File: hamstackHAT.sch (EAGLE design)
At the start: 14 parts, among them K2 RASPI_HEADER, U1 TXB0108PWR

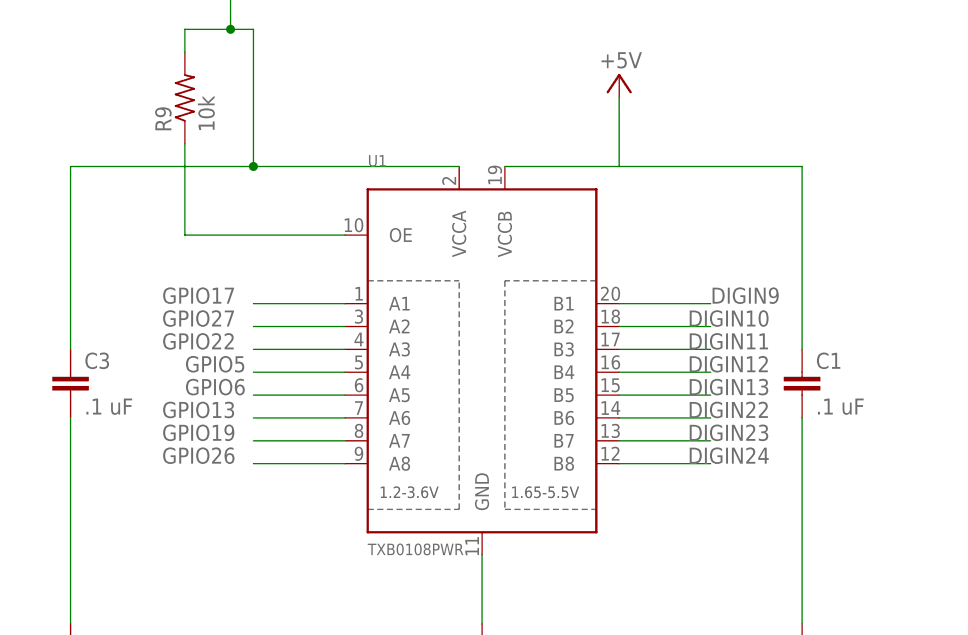
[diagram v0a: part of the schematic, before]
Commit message: re-arange everythign to imporove routing
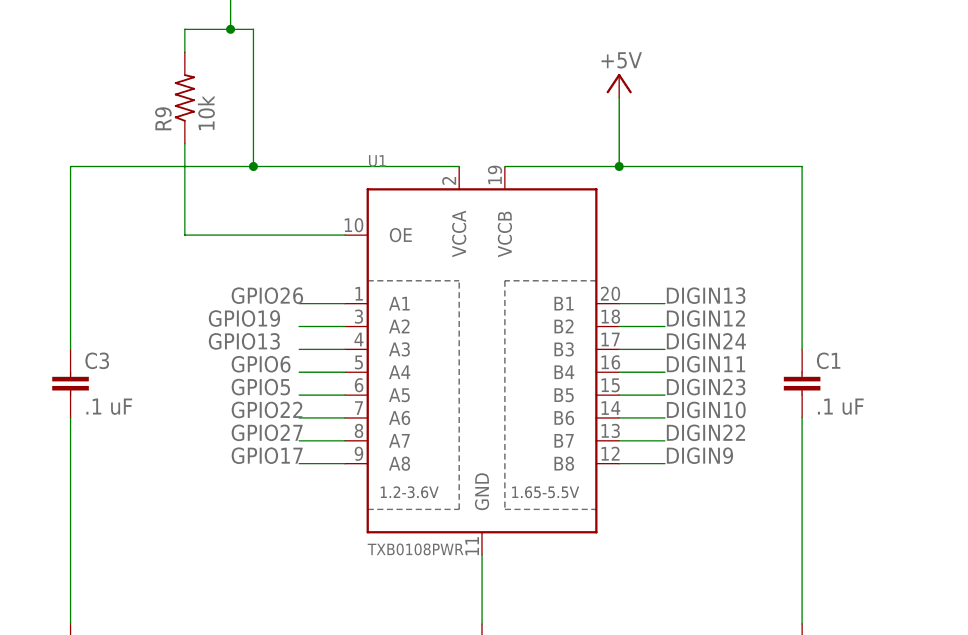
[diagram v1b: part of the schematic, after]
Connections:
- net DIGIN10: now also U1.B6; no longer U1.B2
- net DIGIN11: now also U1.B4; no longer U1.B3
- net DIGIN12: now also U1.B2; no longer U1.B4
- net DIGIN13: now also U1.B1; no longer U1.B5
- net DIGIN22: now also U1.B7; no longer U1.B6
- net DIGIN23: now also U1.B5; no longer U1.B7
- net DIGIN24: now also U1.B3; no longer U1.B8
- net DIGIN9: now also U1.B8; no longer U1.B1
- net GPIO13: now also U1.A3; no longer U1.A6
- net GPIO17: now also U1.A8; no longer U1.A1
- net GPIO19: now also U1.A2; no longer U1.A7
- net GPIO22: now also U1.A6; no longer U1.A3
- net GPIO26: now also U1.A1; no longer U1.A8
- net GPIO27: now also U1.A7; no longer U1.A2
- net GPIO5: now also U1.A5; no longer U1.A4
- net GPIO6: now also U1.A4; no longer U1.A5
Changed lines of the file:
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@@
 <pinref part="P+2" gate="1" pin="+5V"/>
 <pinref part="C1" gate="G$1" pin="1"/>
+<junction x="182.88" y="139.7"/>
 </segment>
 </net>
@@
 </segment>
 <segment>
-<wire x1="182.88" y1="124.46" x2="193.04" y2="124.46" width="0.1524" layer="91"/>
-<pinref part="U1" gate="G$1" pin="B1"/>
-<label x="193.04" y="124.46" size="1.778" layer="95"/>
+<pinref part="U1" gate="G$1" pin="B8"/>
+<wire x1="182.88" y1="106.68" x2="187.96" y2="106.68" width="0.1524" layer="91"/>
+<label x="187.96" y="106.68" size="1.778" layer="95"/>
 </segment>
 </net>
@@
 </segment>
 <segment>
-<wire x1="182.88" y1="121.92" x2="193.04" y2="121.92" width="0.1524" layer="91"/>
-<pinref part="U1" gate="G$1" pin="B2"/>
-<label x="190.5" y="121.92" size="1.778" layer="95"/>
+<pinref part="U1" gate="G$1" pin="B6"/>
+<wire x1="182.88" y1="111.76" x2="187.96" y2="111.76" width="0.1524" layer="91"/>
+<label x="187.96" y="111.76" size="1.778" layer="95"/>
 </segment>
 </net>
@@
 </segment>
 <segment>
-<wire x1="182.88" y1="116.84" x2="193.04" y2="116.84" width="0.1524" layer="91"/>
-<pinref part="U1" gate="G$1" pin="B4"/>
-<label x="190.5" y="116.84" size="1.778" layer="95"/>
+<pinref part="U1" gate="G$1" pin="B2"/>
+<wire x1="182.88" y1="121.92" x2="187.96" y2="121.92" width="0.1524" layer="91"/>
+<label x="187.96" y="121.92" size="1.778" layer="95"/>
 </segment>
 </net>
@@
 </segment>
 <segment>
-<wire x1="182.88" y1="114.3" x2="193.04" y2="114.3" width="0.1524" layer="91"/>
-<pinref part="U1" gate="G$1" pin="B5"/>
-<label x="190.5" y="114.3" size="1.778" layer="95"/>
+<pinref part="U1" gate="G$1" pin="B1"/>
+<wire x1="182.88" y1="124.46" x2="187.96" y2="124.46" width="0.1524" layer="91"/>
+<label x="187.96" y="124.46" size="1.778" layer="95"/>
 </segment>
 </net>
@@
 </segment>
 <segment>
-<wire x1="182.88" y1="109.22" x2="193.04" y2="109.22" width="0.1524" layer="91"/>
-<pinref part="U1" gate="G$1" pin="B7"/>
-<label x="190.5" y="109.22" size="1.778" layer="95"/>
+<pinref part="U1" gate="G$1" pin="B5"/>
+<wire x1="182.88" y1="114.3" x2="187.96" y2="114.3" width="0.1524" layer="91"/>
+<label x="187.96" y="114.3" size="1.778" layer="95"/>
 </segment>
 </net>
@@
 </segment>
 <segment>
-<wire x1="182.88" y1="106.68" x2="193.04" y2="106.68" width="0.1524" layer="91"/>
-<pinref part="U1" gate="G$1" pin="B8"/>
-<label x="190.5" y="106.68" size="1.778" layer="95"/>
+<pinref part="U1" gate="G$1" pin="B3"/>
+<wire x1="182.88" y1="119.38" x2="187.96" y2="119.38" width="0.1524" layer="91"/>
+<label x="187.96" y="119.38" size="1.778" layer="95"/>
 </segment>
 </net>
@@
 </segment>
 <segment>
-<wire x1="182.88" y1="119.38" x2="193.04" y2="119.38" width="0.1524" layer="91"/>
-<pinref part="U1" gate="G$1" pin="B3"/>
-<label x="190.5" y="119.38" size="1.778" layer="95"/>
+<pinref part="U1" gate="G$1" pin="B4"/>
+<wire x1="182.88" y1="116.84" x2="187.96" y2="116.84" width="0.1524" layer="91"/>
+<label x="187.96" y="116.84" size="1.778" layer="95"/>
 </segment>
 </net>
 <net name="DIGIN22" class="0">
-<segment>
-<wire x1="182.88" y1="111.76" x2="193.04" y2="111.76" width="0.1524" layer="91"/>
-<pinref part="U1" gate="G$1" pin="B6"/>
-<label x="190.5" y="111.76" size="1.778" layer="95"/>
-</segment>
 <segment>
 <pinref part="X1" gate="G$1" pin="22"/>
@@
 <label x="152.4" y="180.34" size="1.778" layer="95"/>
 </segment>
+<segment>
+<pinref part="U1" gate="G$1" pin="B7"/>
+<wire x1="182.88" y1="109.22" x2="187.96" y2="109.22" width="0.1524" layer="91"/>
+<label x="187.96" y="109.22" size="1.778" layer="95"/>
+</segment>
 </net>
 <net name="GPIO27" class="0">
-<segment>
-<wire x1="152.4" y1="121.92" x2="142.24" y2="121.92" width="0.1524" layer="91"/>
-<pinref part="U1" gate="G$1" pin="A2"/>
-<label x="132.08" y="121.92" size="1.778" layer="95"/>
-</segment>
 <segment>
 <pinref part="K2" gate="G$1" pin="13"/>
@@
 <label x="10.16" y="160.02" size="1.778" layer="95"/>
 </segment>
+<segment>
+<pinref part="U1" gate="G$1" pin="A7"/>
+<wire x1="147.32" y1="109.22" x2="152.4" y2="109.22" width="0.1524" layer="91"/>
+<label x="139.7" y="109.22" size="1.778" layer="95"/>
+</segment>
 </net>
 <net name="GPIO22" class="0">
-<segment>
-<wire x1="152.4" y1="119.38" x2="142.24" y2="119.38" width="0.1524" layer="91"/>
-<pinref part="U1" gate="G$1" pin="A3"/>
-<label x="132.08" y="119.38" size="1.778" layer="95"/>
-</segment>
 <segment>
 <pinref part="K2" gate="G$1" pin="15"/>
@@
 <label x="7.62" y="157.48" size="1.778" layer="95"/>
 </segment>
+<segment>
+<pinref part="U1" gate="G$1" pin="A6"/>
+<wire x1="147.32" y1="111.76" x2="152.4" y2="111.76" width="0.1524" layer="91"/>
+<label x="139.7" y="111.76" size="1.778" layer="95"/>
+</segment>
 </net>
 <net name="GPIO5" class="0">
-<segment>
-<wire x1="152.4" y1="116.84" x2="142.24" y2="116.84" width="0.1524" layer="91"/>
-<pinref part="U1" gate="G$1" pin="A4"/>
-<label x="134.62" y="116.84" size="1.778" layer="95"/>
-</segment>
 <segment>
 <pinref part="K2" gate="G$1" pin="29"/>
@@
 <label x="10.16" y="139.7" size="1.778" layer="95"/>
 </segment>
+<segment>
+<pinref part="U1" gate="G$1" pin="A5"/>
+<wire x1="147.32" y1="114.3" x2="152.4" y2="114.3" width="0.1524" layer="91"/>
+<label x="139.7" y="114.3" size="1.778" layer="95"/>
+</segment>
 </net>
 <net name="GPIO6" class="0">
-<segment>
-<wire x1="152.4" y1="114.3" x2="142.24" y2="114.3" width="0.1524" layer="91"/>
-<pinref part="U1" gate="G$1" pin="A5"/>
-<label x="134.62" y="114.3" size="1.778" layer="95"/>
-</segment>
 <segment>
 <pinref part="K2" gate="G$1" pin="31"/>
@@
 <label x="12.7" y="137.16" size="1.778" layer="95"/>
 </segment>
+<segment>
+<pinref part="U1" gate="G$1" pin="A4"/>
+<wire x1="147.32" y1="116.84" x2="152.4" y2="116.84" width="0.1524" layer="91"/>
+<label x="139.7" y="116.84" size="1.778" layer="95"/>
+</segment>
 </net>
 <net name="GPIO13" class="0">
-<segment>
-<wire x1="152.4" y1="111.76" x2="142.24" y2="111.76" width="0.1524" layer="91"/>
-<pinref part="U1" gate="G$1" pin="A6"/>
-<label x="132.08" y="111.76" size="1.778" layer="95"/>
-</segment>
 <segment>
 <pinref part="K2" gate="G$1" pin="33"/>
@@
 <label x="7.62" y="134.62" size="1.778" layer="95"/>
 </segment>
+<segment>
+<pinref part="U1" gate="G$1" pin="A3"/>
+<wire x1="147.32" y1="119.38" x2="152.4" y2="119.38" width="0.1524" layer="91"/>
+<label x="137.16" y="119.38" size="1.778" layer="95"/>
+</segment>
 </net>
 <net name="GPIO19" class="0">
-<segment>
-<wire x1="152.4" y1="109.22" x2="142.24" y2="109.22" width="0.1524" layer="91"/>
-<pinref part="U1" gate="G$1" pin="A7"/>
-<label x="132.08" y="109.22" size="1.778" layer="95"/>
-</segment>
 <segment>
 <pinref part="K2" gate="G$1" pin="35"/>
@@
 <label x="10.16" y="132.08" size="1.778" layer="95"/>
 </segment>
+<segment>
+<pinref part="U1" gate="G$1" pin="A2"/>
+<wire x1="147.32" y1="121.92" x2="152.4" y2="121.92" width="0.1524" layer="91"/>
+<label x="137.16" y="121.92" size="1.778" layer="95"/>
+</segment>
 </net>
 <net name="GPIO26" class="0">
-<segment>
-<wire x1="152.4" y1="106.68" x2="142.24" y2="106.68" width="0.1524" layer="91"/>
-<pinref part="U1" gate="G$1" pin="A8"/>
-<label x="132.08" y="106.68" size="1.778" layer="95"/>
-</segment>
 <segment>
 <pinref part="K2" gate="G$1" pin="37"/>
 <wire x1="43.18" y1="129.54" x2="15.24" y2="129.54" width="0.1524" layer="91"/>
 <label x="10.16" y="129.54" size="1.778" layer="95"/>
+</segment>
+<segment>
+<pinref part="U1" gate="G$1" pin="A1"/>
+<wire x1="147.32" y1="124.46" x2="152.4" y2="124.46" width="0.1524" layer="91"/>
+<label x="139.7" y="124.46" size="1.778" layer="95"/>
 </segment>
 </net>
@@
 <net name="GPIO17" class="0">
 <segment>
-<pinref part="U1" gate="G$1" pin="A1"/>
-<wire x1="152.4" y1="124.46" x2="142.24" y2="124.46" width="0.1524" layer="91"/>
-<label x="132.08" y="124.46" size="1.778" layer="95"/>
-</segment>
-<segment>
 <pinref part="K2" gate="G$1" pin="11"/>
 <wire x1="43.18" y1="162.56" x2="17.78" y2="162.56" width="0.1524" layer="91"/>
 <label x="10.16" y="162.56" size="1.778" layer="95"/>
 </segment>
+<segment>
+<pinref part="U1" gate="G$1" pin="A8"/>
+<wire x1="152.4" y1="106.68" x2="147.32" y2="106.68" width="0.1524" layer="91"/>
+<label x="139.7" y="106.68" size="1.778" layer="95"/>
+</segment>
 </net>
 </nets>
 </sheet>
 </sheets>
+<errors>
+</errors>
 </schematic>
 </drawing>

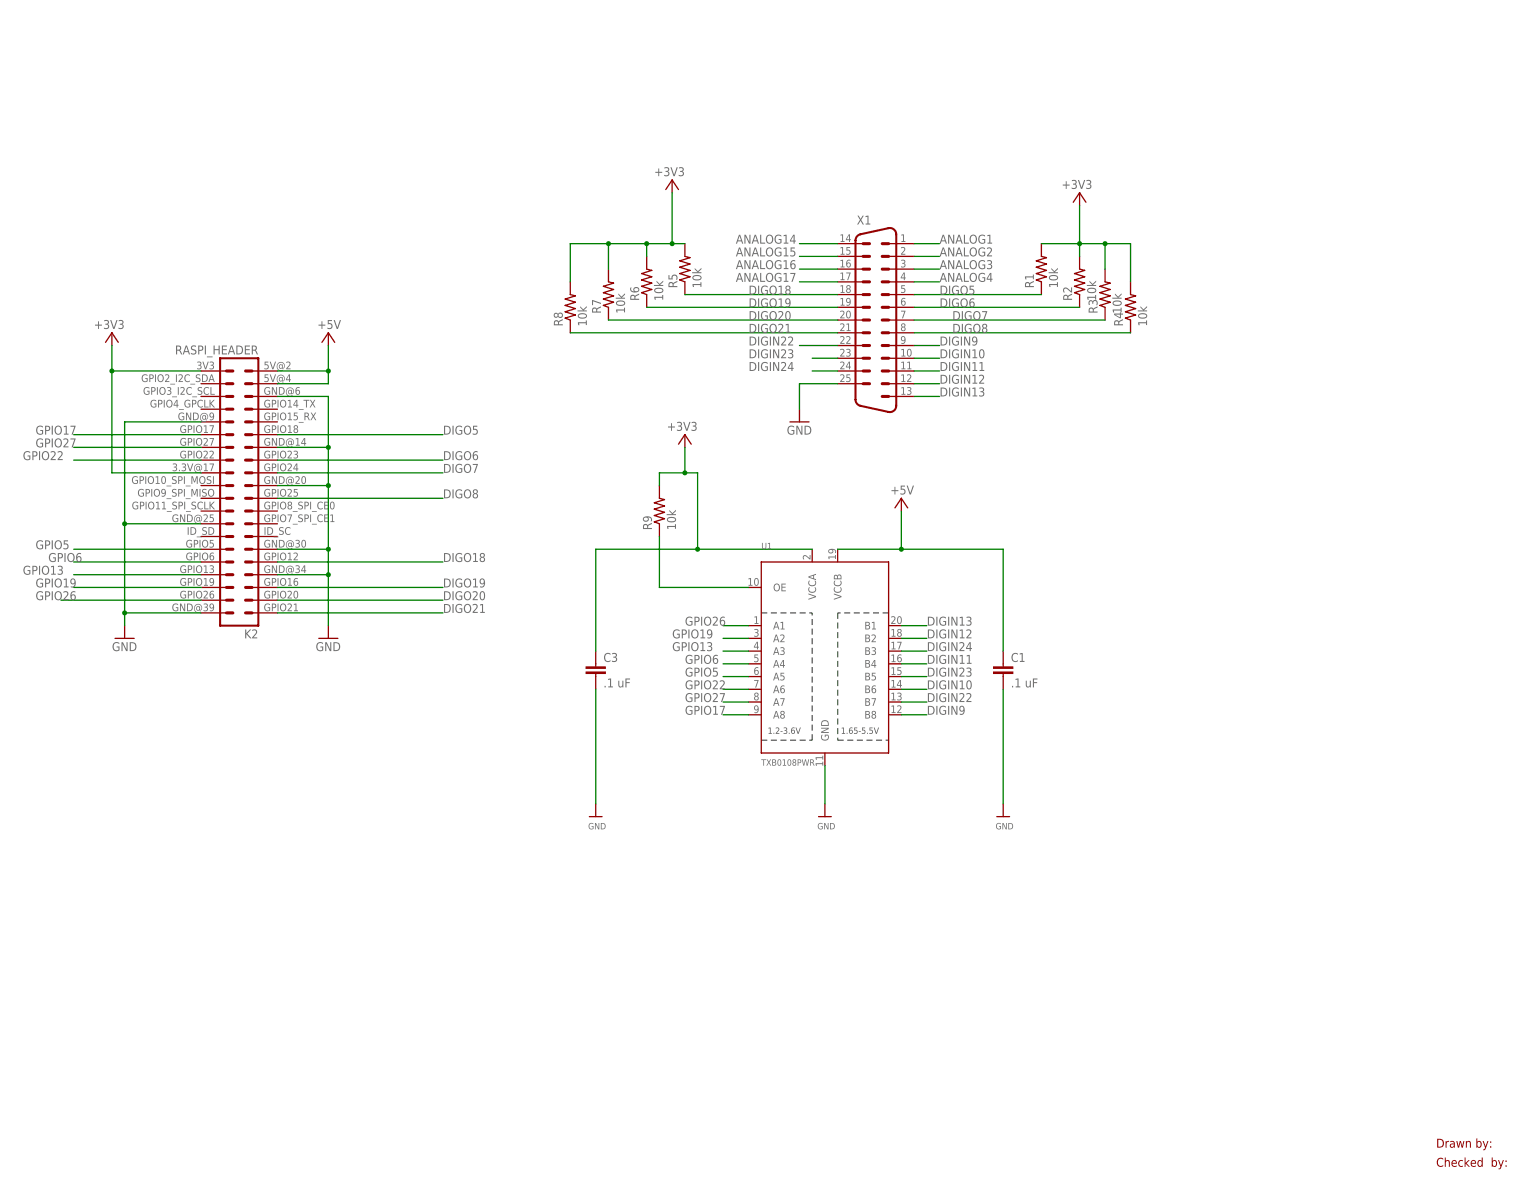
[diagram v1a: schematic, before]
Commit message: tidy up schematic for letter paper
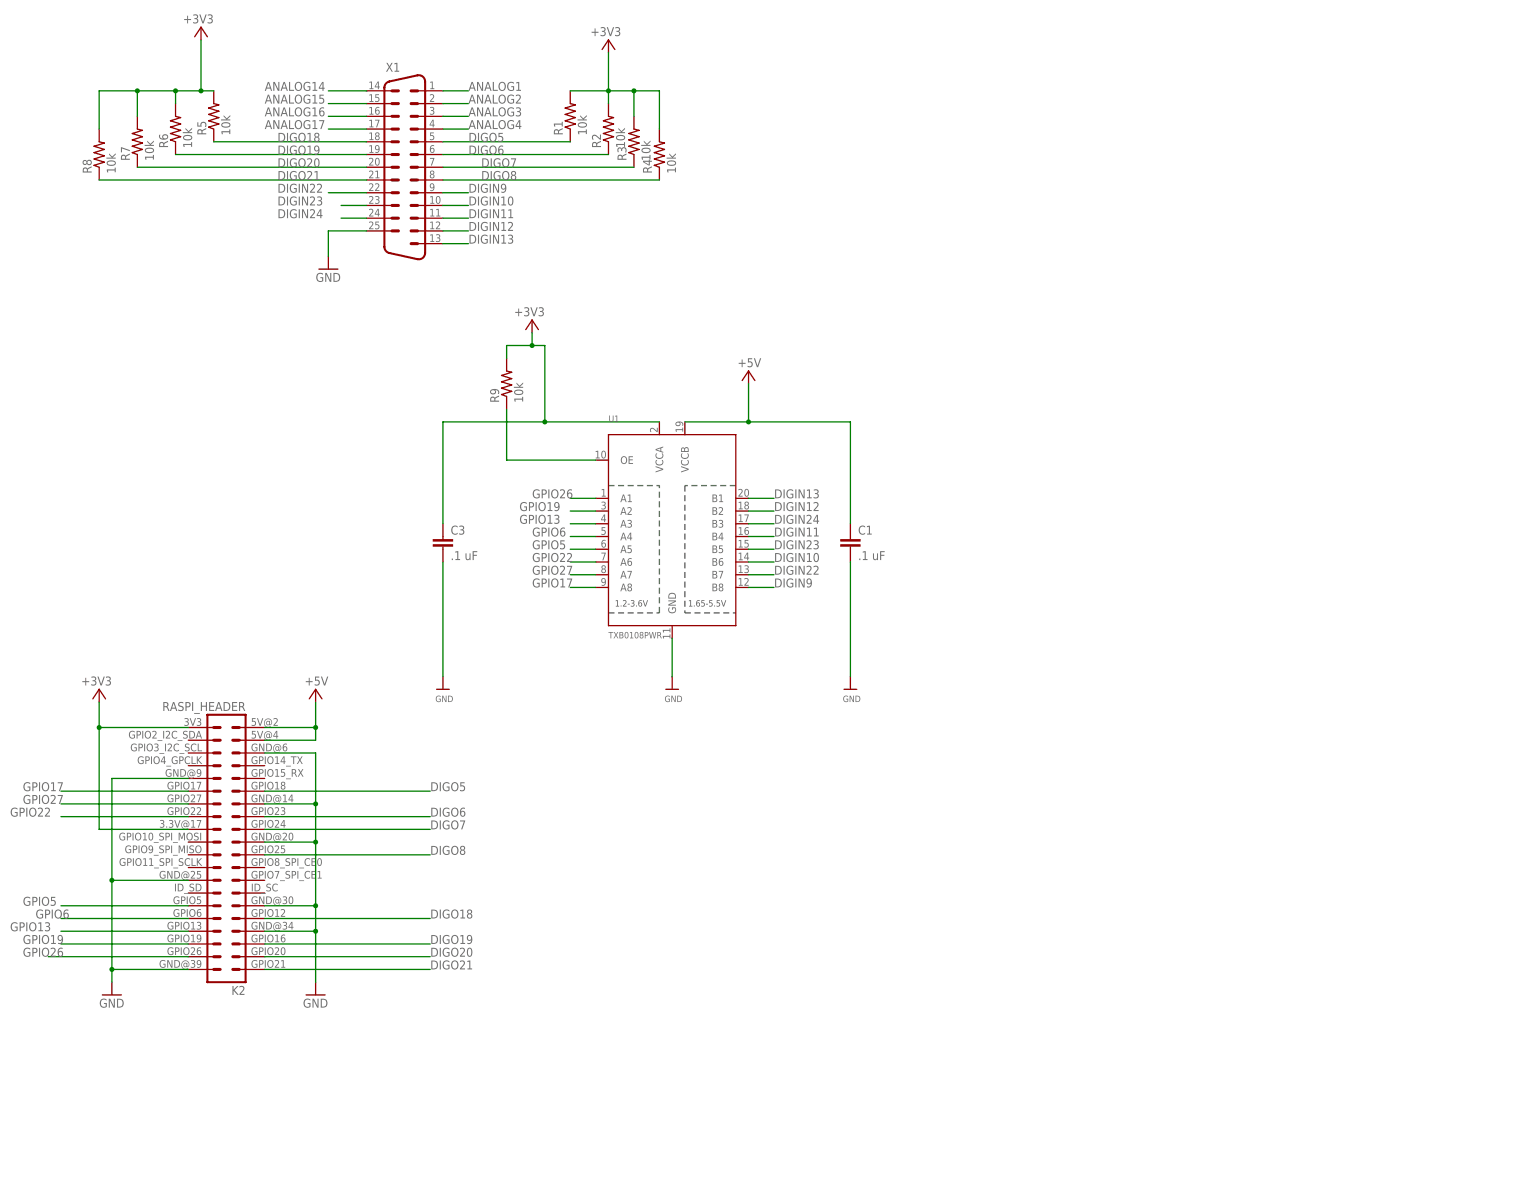
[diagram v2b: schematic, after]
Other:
- note removed: "Checked by:"
- note removed: "Drawn by:"
- moved on the sheet: C1, C3, K2, R1, R2, R3, R4, R5, R6, R7, R8, R9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
